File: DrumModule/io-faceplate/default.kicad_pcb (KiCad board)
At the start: 2 copper layers, 40 x 129 mm, 0 parts

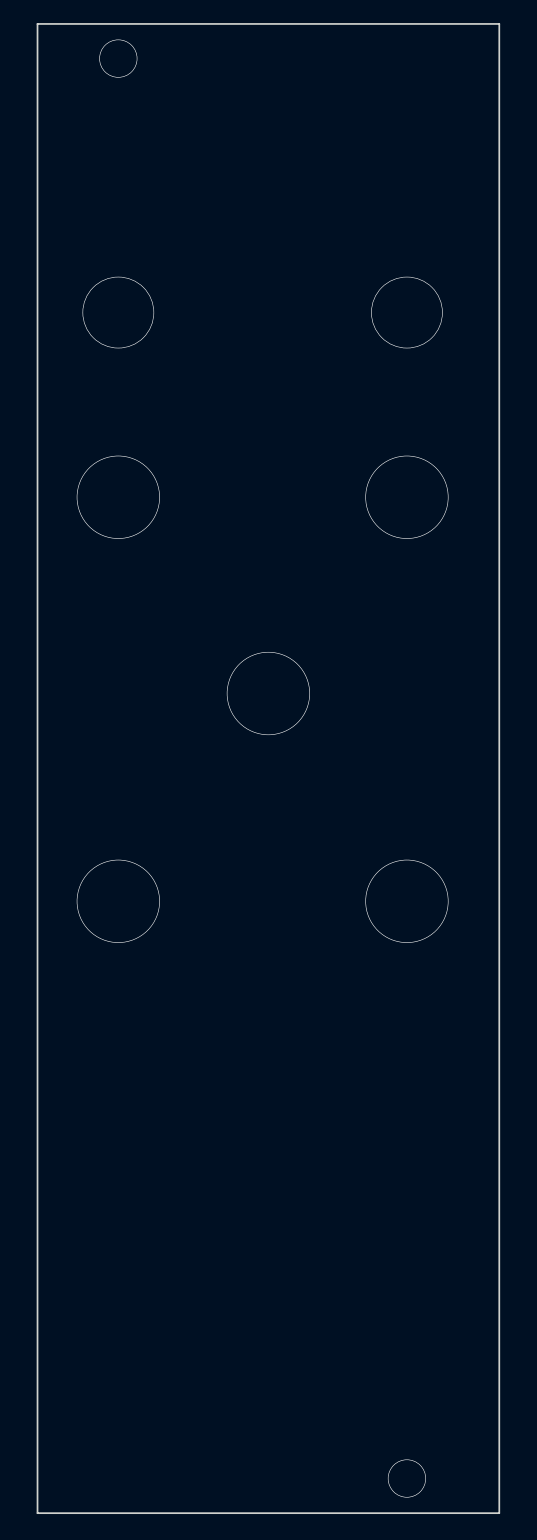
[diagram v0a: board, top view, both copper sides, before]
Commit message: Fit check on the drum and logiccrusher
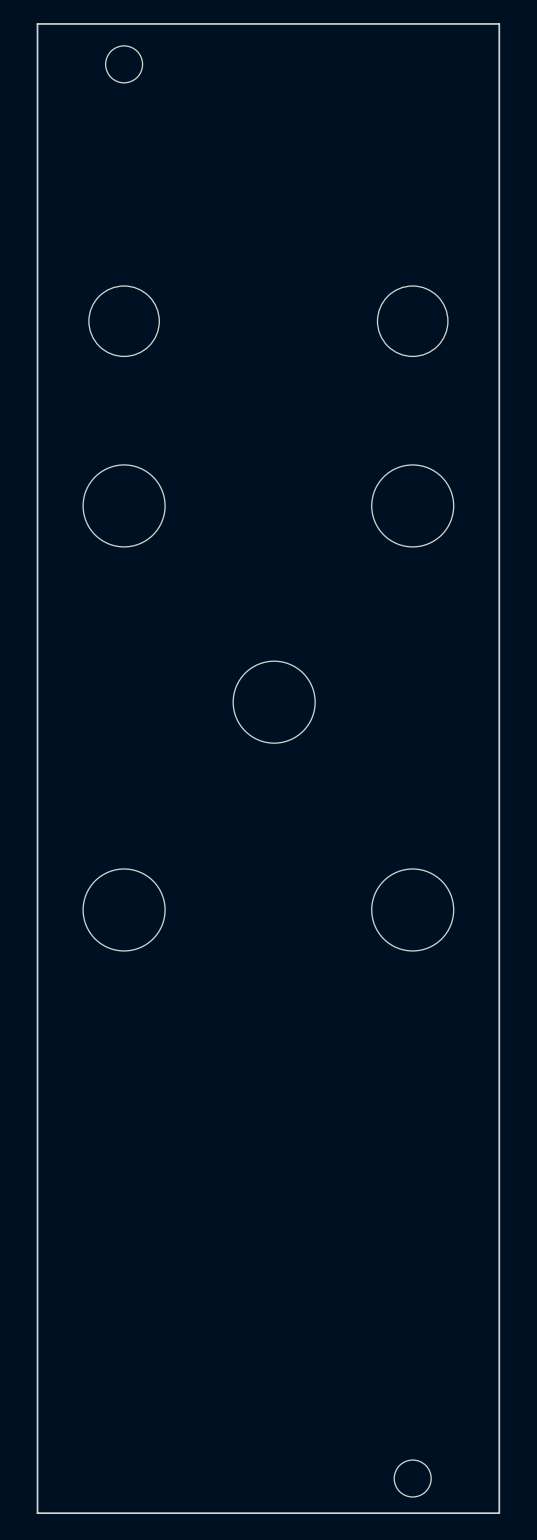
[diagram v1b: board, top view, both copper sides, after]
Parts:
- added ?: , MountingHole:MountingHole_3.5mm, F.Cu at (157.5, 24.5)
- added ?: , MountingHole:MountingHole_3.5mm, F.Cu at (182.5, 147.0)
- added ?: , MountingHole:MountingHole_3.5mm, F.Cu at (157.5, 97.8)
- added ?: , MountingHole:MountingHole_3.5mm, F.Cu at (182.5, 97.8)
- added ?: , MountingHole:MountingHole_3.5mm, F.Cu at (170.5, 79.8)
- added ?: , MountingHole:MountingHole_3.5mm, F.Cu at (157.5, 62.8)
- added ?: , MountingHole:MountingHole_3.5mm, F.Cu at (182.5, 62.8)
- added ?: , MountingHole:MountingHole_3.5mm, F.Cu at (157.5, 46.8)
- added ?: , MountingHole:MountingHole_3.5mm, F.Cu at (182.5, 46.8)
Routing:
- net (no net): vias 9 -> 0
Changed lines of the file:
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@@
     (uvia_drill 0.1)
   )
-(gr_line (start 150 150) (end 150 21) (layer Edge.Cuts) (width 0.15))(gr_line (start 150 21) (end 190 21) (layer Edge.Cuts) (width 0.15))(gr_line (start 190 21) (end 190 150) (layer Edge.Cuts) (width 0.15))(gr_line (start 190 150) (end 150 150) (layer Edge.Cuts) (width 0.15))(via (at 157 24) (size 3.300000) (drill 3.200000) (layers F.Cu B.Cu) (net 0))(via (at 182 147) (size 3.300000) (drill 3.200000) (layers F.Cu B.Cu) (net 0))(gr_line (start 150 30) (end 190 30) (layer Dwgs.User) (width 0.15))(gr_line (start 150 140) (end 190 140) (layer Dwgs.User) (width 0.15))(gr_line (start 150 134) (end 150 36) (layer Dwgs.User) (width 0.15))(gr_line (start 150 36) (end 189 36) (layer Dwgs.User) (width 0.15))(gr_line (start 189 36) (end 189 134) (layer Dwgs.User) (width 0.15))(gr_line (start 150 134) (end 189 134) (layer Dwgs.User) (width 0.15))(via (at 157 97) (size 7.200000) (drill 7.100000) (layers F.Cu B.Cu) (net 0))(via (at 182 97) (size 7.200000) (drill 7.100000) (layers F.Cu B.Cu) (net 0))(via (at 170 79) (size 7.200000) (drill 7.100000) (layers F.Cu B.Cu) (net 0))(via (at 157 62) (size 7.200000) (drill 7.100000) (layers F.Cu B.Cu) (net 0))(via (at 182 62) (size 7.200000) (drill 7.100000) (layers F.Cu B.Cu) (net 0))(via (at 157 46) (size 6.200000) (drill 6.100000) (layers F.Cu B.Cu) (net 0))(via (at 182 46) (size 6.200000) (drill 6.100000) (layers F.Cu B.Cu) (net 0)))
+(gr_line (start 150 150) (end 150 21) (layer Edge.Cuts) (width 0.15))
+(gr_line (start 150 21) (end 190 21) (layer Edge.Cuts) (width 0.15))
+(gr_line (start 190 21) (end 190 150) (layer Edge.Cuts) (width 0.15))
+(gr_line (start 190 150) (end 150 150) (layer Edge.Cuts) (width 0.15))
+(module MountingHole:MountingHole_3.5mm (layer F.Cu)
+(at 157.500000 24.500000)
+(pad 1 np_thru_hole circle (at 0 0) (size 3.200000 3.200000) (drill 3.200000) (layers *.Cu *.Mask))
+)
+(module MountingHole:MountingHole_3.5mm (layer F.Cu)
+(at 182.500000 147.000000)
+(pad 1 np_thru_hole circle (at 0 0) (size 3.200000 3.200000) (drill 3.200000) (layers *.Cu *.Mask))
+)
+(gr_line (start 150 30) (end 190 30) (layer Dwgs.User) (width 0.15))
+(gr_line (start 150 140) (end 190 140) (layer Dwgs.User) (width 0.15))
+(gr_line (start 150 134) (end 150 36) (layer Dwgs.User) (width 0.15))
+(gr_line (start 150 36) (end 189 36) (layer Dwgs.User) (width 0.15))
+(gr_line (start 189 36) (end 189 134) (layer Dwgs.User) (width 0.15))
+(gr_line (start 150 134) (end 189 134) (layer Dwgs.User) (width 0.15))
+(module MountingHole:MountingHole_3.5mm (layer F.Cu)
+(at 157.500000 97.750000)
+(pad 1 np_thru_hole circle (at 0 0) (size 7.100000 7.100000) (drill 7.100000) (layers *.Cu *.Mask))
+)
+(module MountingHole:MountingHole_3.5mm (layer F.Cu)
+(at 182.500000 97.750000)
+(pad 1 np_thru_hole circle (at 0 0) (size 7.100000 7.100000) (drill 7.100000) (layers *.Cu *.Mask))
+)
+(module MountingHole:MountingHole_3.5mm (layer F.Cu)
+(at 170.500000 79.750000)
+(pad 1 np_thru_hole circle (at 0 0) (size 7.100000 7.100000) (drill 7.100000) (layers *.Cu *.Mask))
+)
+(module MountingHole:MountingHole_3.5mm (layer F.Cu)
+(at 157.500000 62.750000)
+(pad 1 np_thru_hole circle (at 0 0) (size 7.100000 7.100000) (drill 7.100000) (layers *.Cu *.Mask))
+)
+(module MountingHole:MountingHole_3.5mm (layer F.Cu)
+(at 182.500000 62.750000)
+(pad 1 np_thru_hole circle (at 0 0) (size 7.100000 7.100000) (drill 7.100000) (layers *.Cu *.Mask))
+)
+(module MountingHole:MountingHole_3.5mm (layer F.Cu)
+(at 157.500000 46.750000)
+(pad 1 np_thru_hole circle (at 0 0) (size 6.100000 6.100000) (drill 6.100000) (layers *.Cu *.Mask))
+)
+(module MountingHole:MountingHole_3.5mm (layer F.Cu)
+(at 182.500000 46.750000)
+(pad 1 np_thru_hole circle (at 0 0) (size 6.100000 6.100000) (drill 6.100000) (layers *.Cu *.Mask))
+)
+)

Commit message: Added some filter calculations
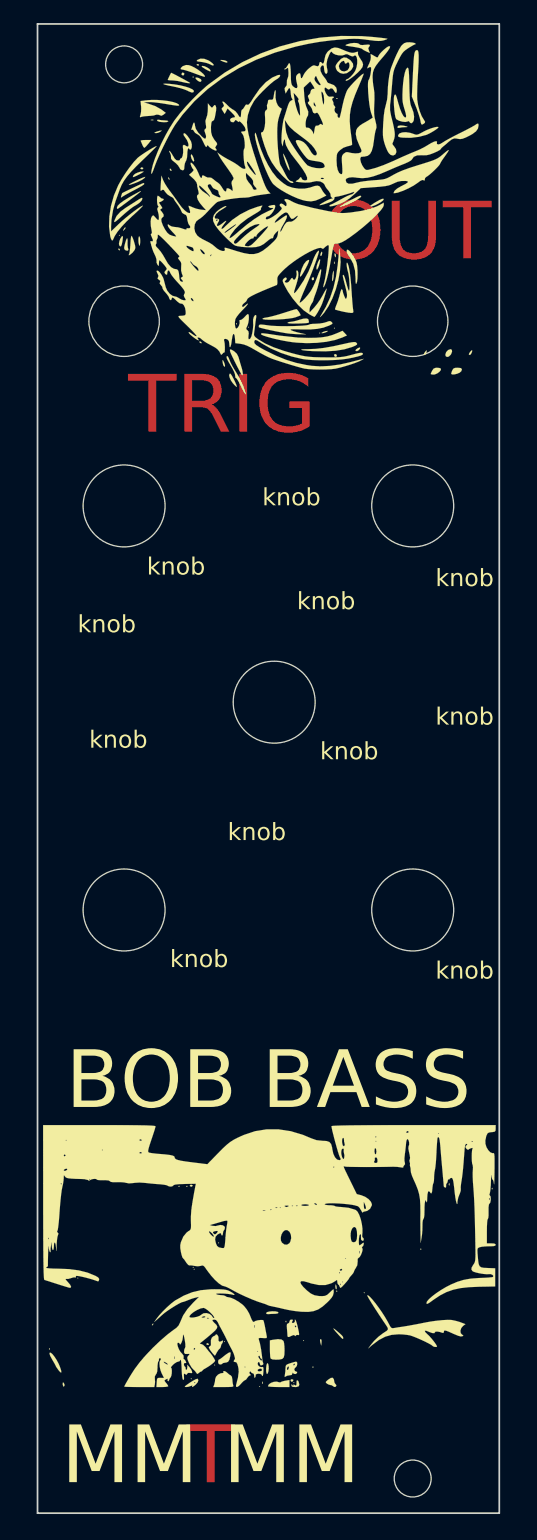
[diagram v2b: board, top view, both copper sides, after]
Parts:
- added ?: , , F.Cu at (167.0, 33.0)
- added ?: , , F.Cu at (172.5, 129.0)
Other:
- board text added: "BOB BASS"
- board text added: "MM MM"
- board text added: "OUT"
- board text added: "T"
- board text added: "TRIG"
- board text added: "knob"
